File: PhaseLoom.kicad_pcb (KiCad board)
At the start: 4 copper layers, 68.8 x 53.6 mm, 77 parts, among them J1 NC, J2 NC, J3 CLK2, J4 Q_OUT, J5 LO_CLK+90, J6 I_OUT, J7 RF_IN, J8 LO_CLK, Q1 AO3400A, Q2 AO3400A, SW1 USR1, SW2 USR2, SW3 USR3, SW4 USR4, SW5 USR5, T1 50:200, U2 ADA4891-2, U3 Si5351A-B-GTR, U4 74CBTLV3253PW, U5 MIC5504-3.3YM5, Y1 25Mhz

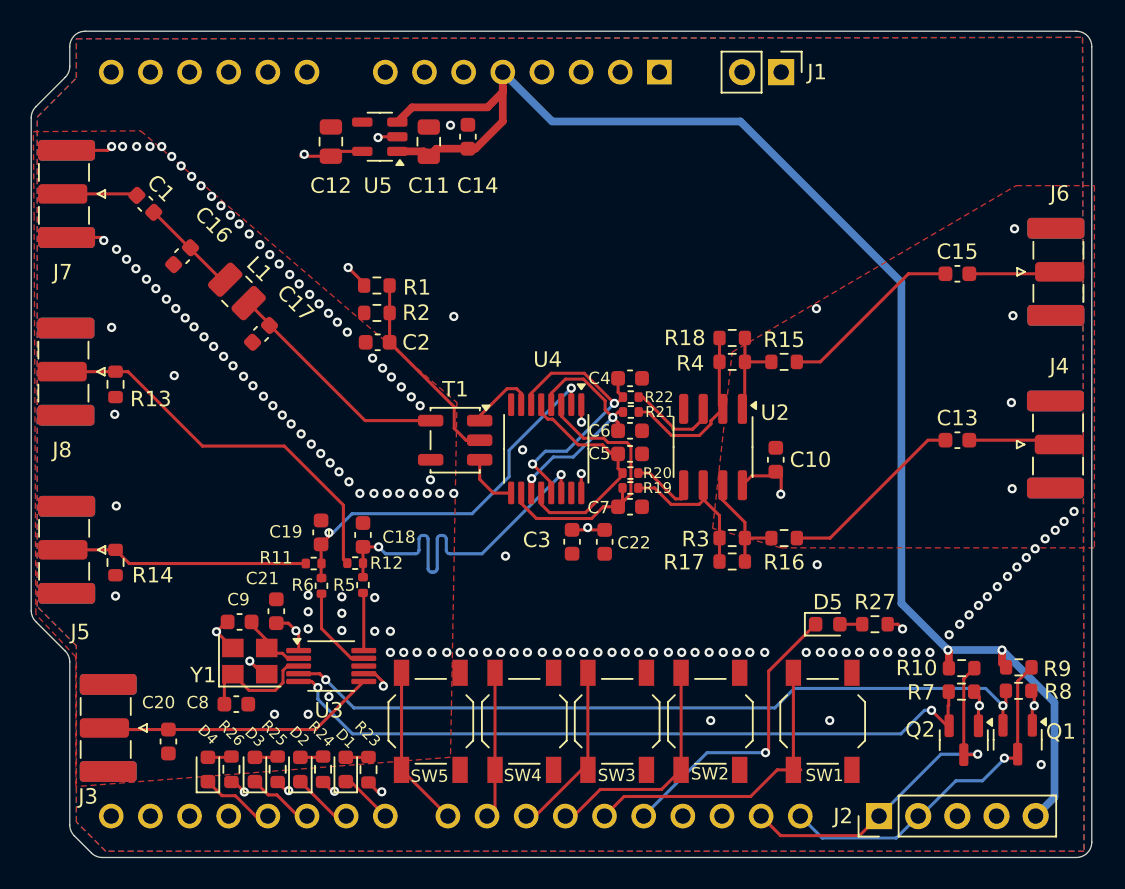
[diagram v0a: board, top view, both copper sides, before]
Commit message: v1.1 Fix: Swap I- and Q-, improve stitching
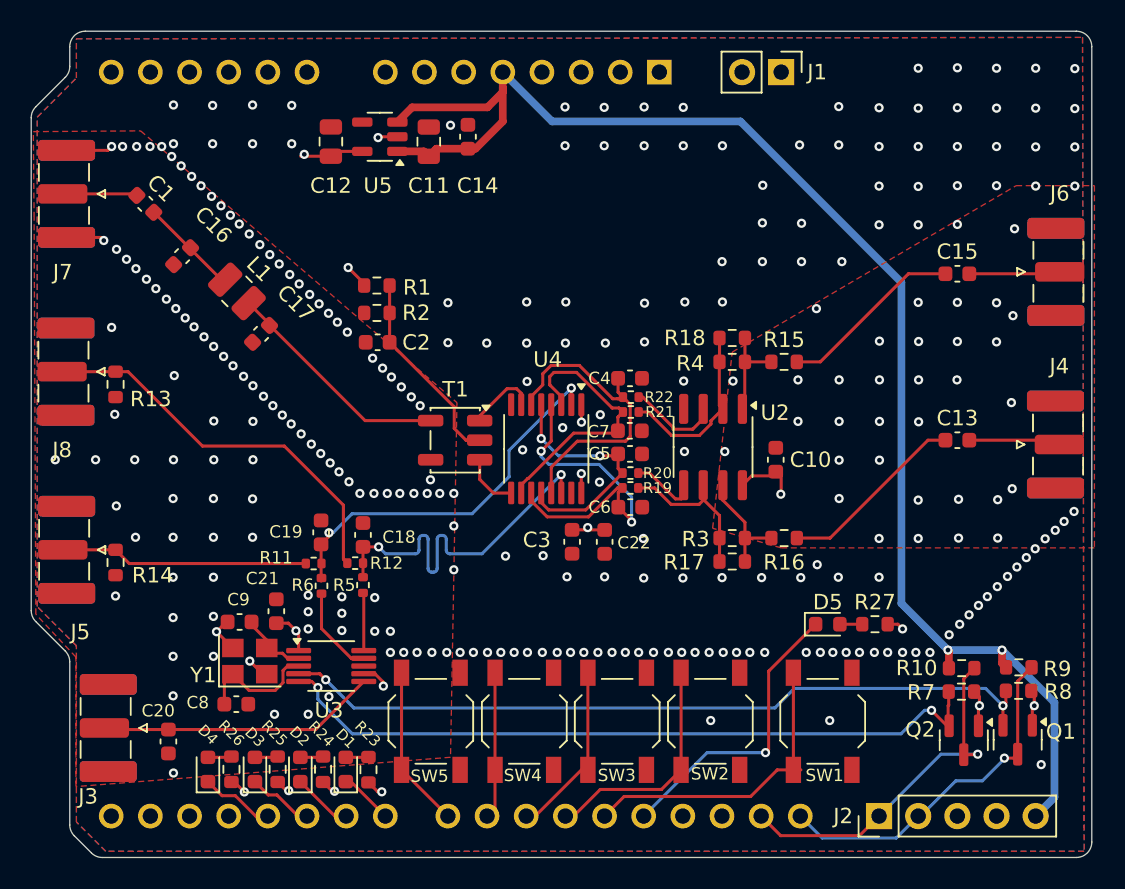
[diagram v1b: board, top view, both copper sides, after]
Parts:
- J5: value LO_CLK+90 -> LO_CLK
- J8: value LO_CLK -> LO_CLK+90
- moved C6 4.95 mm to (161.7, 117.4)
- moved C7 4.93 mm to (161.6, 112.4)
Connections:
- net /+90 renamed /CLK1
- net /LO renamed /CLK0
- C6 pad 2: /I- -> /Q-
- C7 pad 2: /Q- -> /I-
- U4 pad 10: /Q- -> /I-
- U4 pad 11: /I- -> /Q-
- U4 pad 3: /Q- -> /I-
- U4 pad 4: /I- -> /Q-
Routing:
- net /Q-: track 18.9 -> 22.5 mm, vias 0 -> 2
- net /I+: track 18.9 -> 20.6 mm, vias 2 -> 0
- net /Q+: track 14.7 -> 16.2 mm, vias 0 -> 2
- net /I-: track 16.6 -> 17.7 mm, vias 2 -> 0
- net GND: vias 151 -> 285
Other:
- board text added: "CLK0"
- board text added: "CLK1"
- board text added: "PhaseLoom v1.1"
- board text removed: "LO (CLK0)"
- board text removed: "LO + 90° (CLK1)"
- board text removed: "PhaseLoom v1.0"
